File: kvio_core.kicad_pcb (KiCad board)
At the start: 6 copper layers, 98 x 30 mm, 269 parts, among them J1001 12-pin_FFC_(SFV12R), J1301 USB3_B_Micro, J301 Conn_01x06_Male, J401 12-pin_FFC_(SFV12R), J801 12-pin_FFC_(SFV12R), J901 12-pin_FFC_(SFV12R), U1001 IP4254CZ8-4-TTL, U1002 EMI8143, U101 xc7a100t-csg324, U102 ASM330LHH, U1101 AR0135CS, U1201 MT41J128M16JT-125:K, U1301 FT601Q, U1302 EMI8143, U1401 AR0135CS, U201 FAN53541, U202 FAN53541, U203 FAN53541, U204 FAN53541, U301 MX25L6433F, U302 MAX809, U401 EMI8143, U402 IP4254CZ8-4-TTL, U801 IP4254CZ8-4-TTL, U802 EMI8143, U901 IP4254CZ8-4-TTL, U902 EMI8143, Y1301 Crystal_GND24_Small

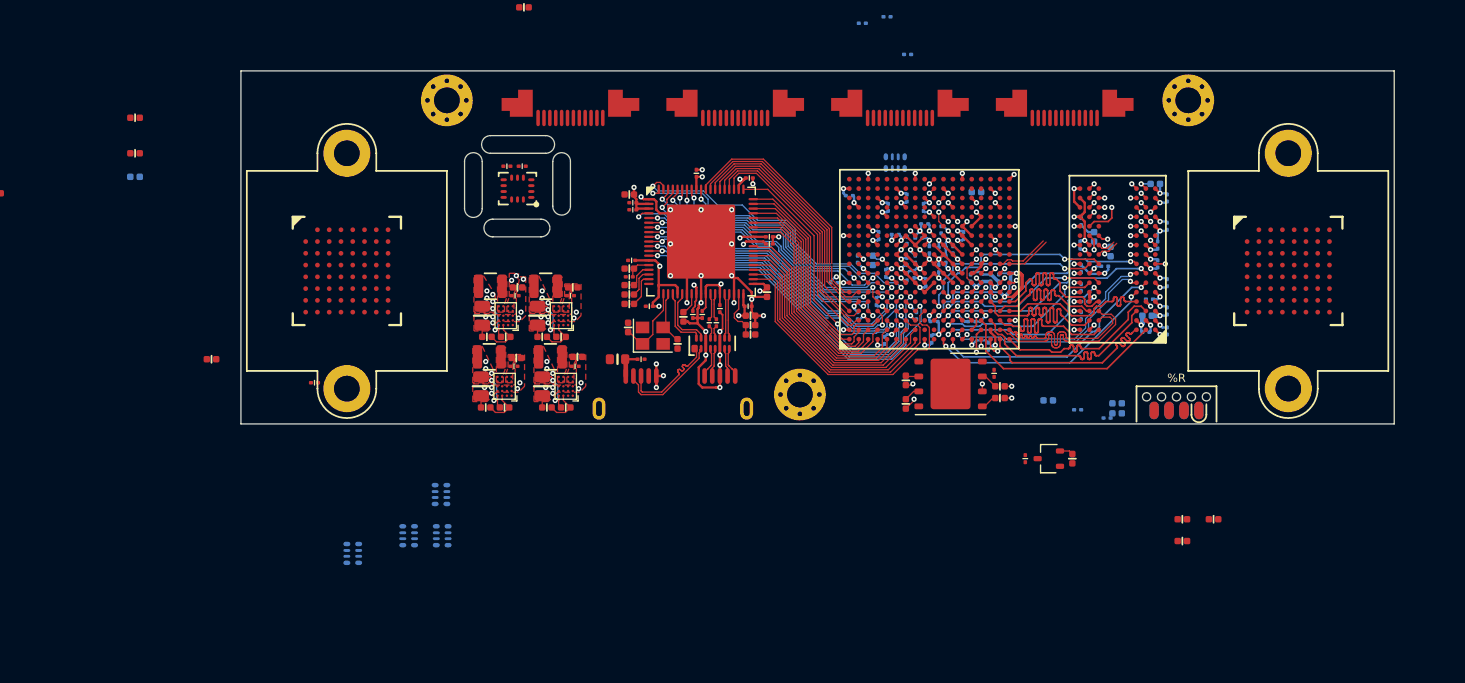
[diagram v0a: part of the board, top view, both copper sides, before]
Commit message: Added IMU + heater, fixed USB3 FIFO lines
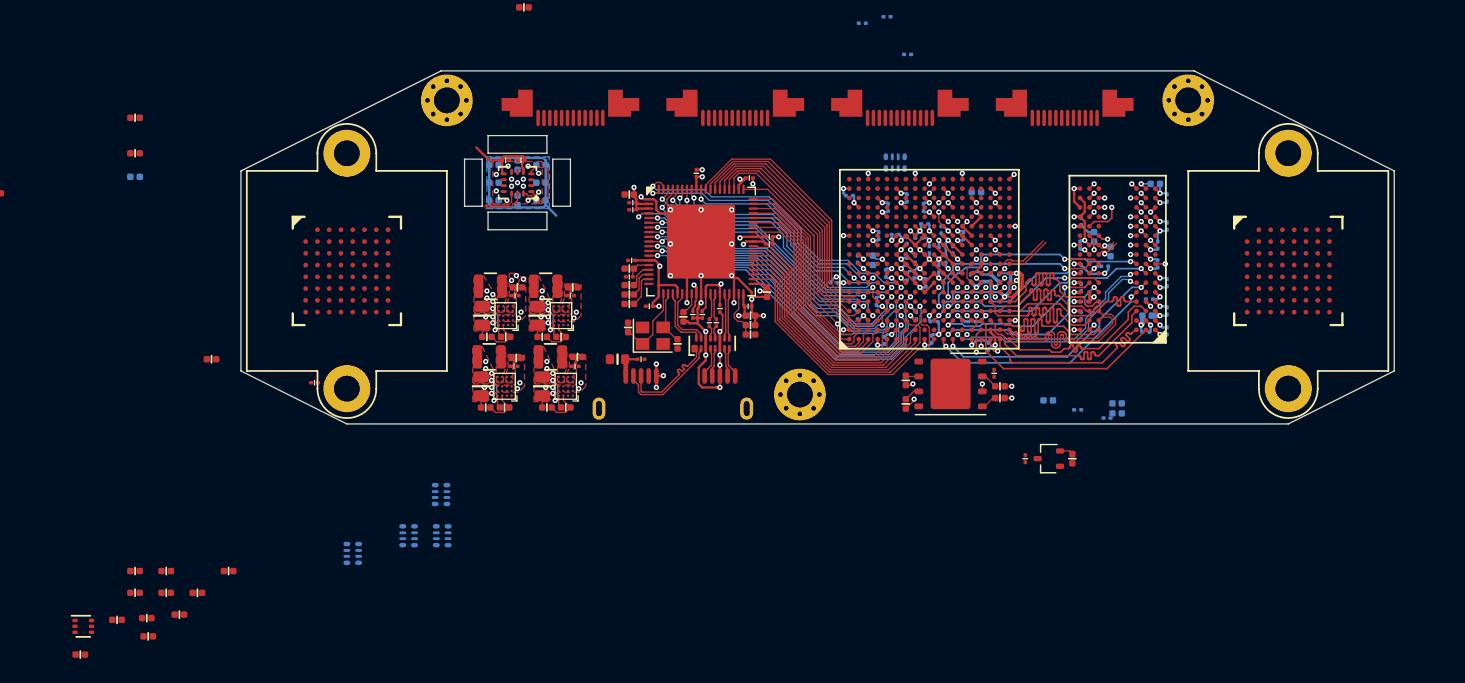
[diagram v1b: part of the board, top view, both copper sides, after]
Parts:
- removed %R: %V, connectors:SOICbiteSmall
- removed C101: 4.7u, passive:C_0402
- removed C102, C103: 0.1u, passive:C_0201
- removed FB101: Ferrite_Bead_Small, passive:R_0402
- removed R101: 4.7k, passive:R_0402
- removed U102: ASM330LHH, lga:LGA-14-2.5x3
- added C1205: 4.7u, passive:C_0402, F.Cu at (139.0, 127.5)
- added C1209: 0.1u, passive:C_0201, F.Cu at (171.8, 92.6)
- added C1222: 0.1u, passive:C_0201, F.Cu at (170.5, 92.6)
- added FB1201: Ferrite_Bead_Small, passive:R_0402, F.Cu at (134.3, 134.6)
- added Q1201: NTZD3155C, sot:SOT-563, F.Cu at (134.6, 132.2)
- added R1206: 100, passive:R_0402, F.Cu at (139.0, 129.3)
- added R1207: 4.7k, passive:R_0402, F.Cu at (137.5, 131.7)
- added R1208: 4.7k, passive:R_0402, F.Cu at (141.7, 127.5)
- added R1209: 180, passive:R_0402, B.Cu at (171.5, 93.0)
- added R1210: 4.7k, passive:R_0402, F.Cu at (141.7, 129.3)
- added R1211: 180, passive:R_0402, B.Cu at (169.5, 94.5)
- added R1212: 180, passive:R_0402, B.Cu at (169.5, 96.0)
- added R1213: 100, passive:R_0402, F.Cu at (140.1, 133.1)
- added R1214: 100, passive:R_0402, F.Cu at (144.3, 129.3)
- added R1215: 100, passive:R_0402, F.Cu at (142.8, 131.2)
- added R1216: 100, passive:R_0402, F.Cu at (146.9, 127.5)
- added R1217: 100, passive:R_0402, F.Cu at (140.0, 131.5)
- added R1218: 180, passive:R_0402, B.Cu at (169.5, 93.0)
- added R1219: 180, passive:R_0402, B.Cu at (173.5, 96.0)
- added R1220: 180, passive:R_0402, B.Cu at (171.5, 96.0)
- added R1221: 180, passive:R_0402, B.Cu at (173.5, 94.5)
- added R1222: 180, passive:R_0402, B.Cu at (173.5, 93.0)
- added U1202: ASM330LHH, lga:LGA-14-2.5x3, F.Cu at (171.5, 94.5)
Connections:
- U101 pad A1: /USB3 Interface/DATA_18 -> /USB3 Interface/DATA_14
- U101 pad A3: /USB3 Interface/DATA_16 -> /USB3 Interface/DATA_17
- U101 pad A4: /USB3 Interface/DATA_15 -> /USB3 Interface/DATA_19
- U101 pad A5: /USB3 Interface/DATA_6 -> /USB3 Interface/DATA_20
- U101 pad A6: /USB3 Interface/DATA_5 -> /USB3 Interface/DATA_22
- U101 pad B1: /USB3 Interface/DATA_17 -> /USB3 Interface/DATA_12
- U101 pad B2: /USB3 Interface/DATA_20 -> /USB3 Interface/DATA_13
- U101 pad B3: /USB3 Interface/DATA_19 -> /USB3 Interface/DATA_16
- U101 pad B4: /USB3 Interface/DATA_14 -> /USB3 Interface/DATA_18
- U101 pad B6: /USB3 Interface/DATA_4 -> /USB3 Interface/DATA_21
- U101 pad B7: /USB3 Interface/DATA_3 -> /USB3 Interface/DATA_23
- U101 pad C1: /USB3 Interface/DATA_31 -> /USB3 Interface/DATA_10
- U101 pad C11: Net-(U101-PadC11) -> /IMU_HEATER
- U101 pad C2: /USB3 Interface/DATA_30 -> /USB3 Interface/DATA_11
- U101 pad C4: /USB3 Interface/DATA_13 -> /USB3 Interface/DATA_28
- U101 pad C5: /USB3 Interface/DATA_2 -> /USB3 Interface/BE_0
- U101 pad C6: /USB3 Interface/DATA_1 -> /USB3 Interface/DATA_29
- U101 pad C7: /USB3 Interface/DATA_8 -> /USB3 Interface/DATA_31
- U101 pad D2: /USB3 Interface/DATA_27 -> /USB3 Interface/DATA_9
- U101 pad D3: /USB3 Interface/DATA_23 -> /USB3 Interface/DATA_15
- U101 pad D4: /USB3 Interface/DATA_22 -> /USB3 Interface/BE_3
- U101 pad D5: /USB3 Interface/DATA_21 -> /USB3 Interface/DATA_26
- U101 pad D7: /USB3 Interface/DATA_12 -> /USB3 Interface/DATA_25
- U101 pad D8: /USB3 Interface/DATA_7 -> /USB3 Interface/DATA_24
- U101 pad E1: /USB3 Interface/BE_3 -> /USB3 Interface/DATA_7
- U101 pad E2: /USB3 Interface/DATA_26 -> /USB3 Interface/DATA_8
- U101 pad E5: /USB3 Interface/DATA_10 -> /USB3 Interface/BE_2
- U101 pad E6: /USB3 Interface/DATA_9 -> /USB3 Interface/BE_1
- U101 pad E7: /USB3 Interface/DATA_11 -> /USB3 Interface/DATA_27
- U101 pad F1: /USB3 Interface/BE_2 -> /USB3 Interface/DATA_6
- U101 pad F3: /USB3 Interface/DATA_25 -> /USB3 Interface/SIWU_N
- U101 pad F4: /USB3 Interface/DATA_24 -> /USB3 Interface/WR_N
- U101 pad F5: /USB3 Interface/DATA_0 -> /USB3 Interface/TXE_N
- U101 pad F6: /USB3 Interface/RXF_N -> /USB3 Interface/DATA_30
- U101 pad G1: /USB3 Interface/BE_1 -> /USB3 Interface/DATA_4
- U101 pad G2: /USB3 Interface/DATA_29 -> /USB3 Interface/DATA_5
- U101 pad G3: /USB3 Interface/WR_N -> /USB3 Interface/DATA_1
- U101 pad G4: /USB3 Interface/SIWU_N -> /USB3 Interface/RXF_N
- U101 pad G6: /USB3 Interface/TXE_N -> /USB3 Interface/RD_N
- U101 pad H1: /USB3 Interface/BE_0 -> /USB3 Interface/DATA_2
- U101 pad H2: /USB3 Interface/DATA_28 -> /USB3 Interface/DATA_3
- U101 pad J4: /USB3 Interface/RD_N -> /USB3 Interface/DATA_0
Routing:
- net /Sensors/IMU_HEATER: track 0.00 -> 19.3 mm
- net /USB3 Interface/DATA_1: track 4.55 -> 23.3 mm, vias 1 -> 0
- net GND: track 145.7 -> 162.0 mm, vias 103 -> 116
- net /USB3 Interface/DATA_3: track 4.87 -> 21.2 mm, vias 1 -> 0
- net /USB3 Interface/DATA_2: track 4.86 -> 20.5 mm, vias 1 -> 0
- net /USB3 Interface/BE_0: track 39.2 -> 24.0 mm, vias 1 -> 2
- net /USB3 Interface/DATA_29: track 37.4 -> 22.4 mm, vias 1 -> 2
- net /USB3 Interface/DATA_5: track 5.51 -> 20.5 mm
- net /USB3 Interface/DATA_0: track 10.6 -> 25.0 mm, vias 1 -> 0
- net /USB3 Interface/DATA_28: track 38.7 -> 24.6 mm, vias 1 -> 2
- net /USB3 Interface/DATA_4: track 6.76 -> 19.8 mm
- net /USB3 Interface/DATA_6: track 6.50 -> 19.1 mm
- net /USB3 Interface/DATA_8: track 9.06 -> 20.6 mm, vias 1 -> 0
- net /USB3 Interface/DATA_7: track 7.45 -> 18.7 mm, vias 1 -> 0
- net /USB3 Interface/BE_1: track 36.9 -> 26.2 mm, vias 1 -> 2
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- added copper zone on B.Cu, net GND
- added copper zone on GND_PWR1, net GND
- added copper zone on GND_PWR3, net GND
- added copper zone on Sig, net GND
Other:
- outline, holes or cut-outs redrawn

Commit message: More layout
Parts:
- added R1105: 1.6k, passive:R_0402, B.Cu at (251.5, 105.7)
- added R1106: 1.6k, passive:R_0402, B.Cu at (254.1, 105.7)
- added R701: 1.6k, passive:R_0402, B.Cu at (151.5, 100.3)
- added R702: 1.6k, passive:R_0402, B.Cu at (151.5, 101.2)
- C1001, C1101, C1102, C1103, C1105, C1106, C1107, C1108, C1109, C1110, C1111, C1112, C1113, C1114, C1115, C1116, C1401, C1402, C1403, C1404, C1405, C1406, C1407, C1408, C1409, C1410, C1411, C1412, C1413, C1414, C1415, C1416, C284, C401, C801, C901, FB1001, FB1101, FB1401, FB401, FB801, FB901, R1001, R1002, R1101, R1102, R1103, R1104, R1402, R801, R802, R901, R902, U1001, U1002, U401, U402, U801, U802, U901, U902: moved to B.Cu
- RN101: moved to F.Cu
- moved C1104 200.7 mm to (251.3, 110.8), turned to 180 degrees
- moved C1107 187.0 mm to (245.2, 118.1), turned to 180 degrees
- moved R1103 186.7 mm to (249.6, 115.0), turned to 180 degrees
- moved FB1101 182.2 mm to (242.6, 118.1), turned to 180 degrees
- moved R1101 181.8 mm to (246.9, 113.2), turned to 180 degrees
- moved R1102 176.9 mm to (244.3, 113.2), turned to 180 degrees
- moved R1104 175.3 mm to (243.1, 107.0), turned to 270 degrees
- moved C1112 168.8 mm to (235.2, 119.8), turned to 180 degrees
- moved C1413 152.4 mm to (260.5, 120.5)
- moved C1414 152.4 mm to (262.8, 120.5)
- moved C1402 152.3 mm to (247.4, 120.4)
- moved C1408 152.3 mm to (250.1, 120.4)
- moved C1401 151.9 mm to (238.5, 120.0)
- moved C1410 150.6 mm to (260.1, 118.7)
- moved C1416 150.6 mm to (257.9, 118.7)
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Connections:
- net Net-(C1001-Pad1) renamed /Camera 4/5V_CAM
- net Net-(C401-Pad1) renamed /Camera 1/5V_CAM
- net Net-(C801-Pad1) renamed /Camera 2/5V_CAM
- net Net-(C901-Pad1) renamed /Camera 3/5V_CAM
- net Net-(J1001-Pad10) renamed /Camera 4/SDA_P
- net Net-(J1001-Pad11) renamed /Camera 4/SCL_P
- net Net-(J1001-Pad2) renamed /Camera 4/D1_P_N
- net Net-(J1001-Pad3) renamed /Camera 4/D1_P_P
- net Net-(J1001-Pad5) renamed /Camera 4/CLK_P_N
- net Net-(J1001-Pad6) renamed /Camera 4/CLK_P_P
- net Net-(J1001-Pad8) renamed /Camera 4/IO1_P
- net Net-(J1001-Pad9) renamed /Camera 4/IO2_P
- net Net-(J401-Pad10) renamed /Camera 1/SDA_P
- net Net-(J401-Pad11) renamed /Camera 1/SCL_P
- net Net-(J401-Pad2) renamed /Camera 1/D1_P_N
- net Net-(J401-Pad3) renamed /Camera 1/D1_P_P
- net Net-(J401-Pad5) renamed /Camera 1/CLK_P_N
- net Net-(J401-Pad6) renamed /Camera 1/CLK_P_P
- net Net-(J401-Pad8) renamed /Camera 1/IO1_P
- net Net-(J401-Pad9) renamed /Camera 1/IO2_P
- net Net-(J801-Pad10) renamed /Camera 2/SDA_P
- net Net-(J801-Pad11) renamed /Camera 2/SCL_P
- net Net-(J801-Pad2) renamed /Camera 2/D1_P_N
- net Net-(J801-Pad3) renamed /Camera 2/D1_P_P
- net Net-(J801-Pad5) renamed /Camera 2/CLK_P_N
- net Net-(J801-Pad6) renamed /Camera 2/CLK_P_P
- net Net-(J801-Pad8) renamed /Camera 2/IO1_P
- net Net-(J801-Pad9) renamed /Camera 2/IO2_P
- net Net-(J901-Pad10) renamed /Camera 3/SDA_P
- net Net-(J901-Pad11) renamed /Camera 3/SCL_P
- net Net-(J901-Pad2) renamed /Camera 3/D1_P_N
- net Net-(J901-Pad3) renamed /Camera 3/D1_P_P
- net Net-(J901-Pad5) renamed /Camera 3/CLK_P_N
- net Net-(J901-Pad6) renamed /Camera 3/CLK_P_P
- net Net-(J901-Pad8) renamed /Camera 3/IO1_P
- net Net-(J901-Pad9) renamed /Camera 3/IO2_P
- net Net-(R1102-Pad1) renamed /sheet5D568411/STANDBY
- net Net-(R1104-Pad1) renamed /sheet5D568411/~OE
- net Net-(R1401-Pad1) renamed /Parallel camera/STANDBY
- net Net-(R1403-Pad1) renamed /Parallel camera/~OE
- RN101 pad 2: /CAM1_CLK_P -> /CAM0_TRIGGER_P
- RN101 pad 3: Net-(RN101-Pad3) -> /CAM1_CLK_P
- RN101 pad 4: Net-(RN101-Pad4) -> /CAM1_TRIGGER_P
- RN101 pad 5: Net-(RN101-Pad5) -> /CAM1_TRIGGER
- RN101 pad 6: Net-(RN101-Pad6) -> /CAM1_CLK
- RN101 pad 7: /CAM1_CLK -> /CAM0_TRIGGER
- RN1101 pad 1: /sheet5D568411/PIXCLK_P -> /CAM1_FLASH
- RN1101 pad 2: Net-(RN1101-Pad2) -> /CAM1_PIXCLK
- RN1101 pad 3: /sheet5D568411/FV_P -> /CAM1_FV
- RN1101 pad 4: /sheet5D568411/LV_P -> /CAM1_LV
- RN1101 pad 5: /CAM1_LV -> /sheet5D568411/LV_P
- RN1101 pad 6: /CAM1_FV -> /sheet5D568411/FV_P
- RN1101 pad 7: Net-(RN1101-Pad7) -> /sheet5D568411/PIXCLK_P
- RN1101 pad 8: /CAM1_PIXCLK -> /sheet5D568411/FLASH_P
- RN1401 pad 1: /Parallel camera/PIXCLK_P -> /CAM0_FLASH
- RN1401 pad 2: Net-(RN1401-Pad2) -> /CAM0_PIXCLK
- RN1401 pad 3: /Parallel camera/FV_P -> /CAM0_FV
- RN1401 pad 4: /Parallel camera/LV_P -> /CAM0_LV
- RN1401 pad 5: /CAM0_LV -> /Parallel camera/LV_P
- RN1401 pad 6: /CAM0_FV -> /Parallel camera/FV_P
- RN1401 pad 7: Net-(RN1401-Pad7) -> /Parallel camera/PIXCLK_P
- RN1401 pad 8: /CAM0_PIXCLK -> /Parallel camera/FLASH_P
- U101 pad B18: /CAM0_TRIGGER -> /CAM0_TRIGGER_P
- U101 pad C16: /CAM1_TRIGGER -> /CAM1_TRIGGER_P
- U101 pad J5: Net-(U101-PadJ5) -> /USB3 Interface/RESET
- U1101 pad E4: /CAM1_FLASH -> /sheet5D568411/FLASH_P
- U1401 pad E4: /CAM0_FLASH -> /Parallel camera/FLASH_P
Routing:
- net +1V8: track 22.0 -> 62.9 mm, vias 16 -> 30
- net /USB3 Interface/RESET: track 2.13 -> 34.8 mm, vias 0 -> 2
- net GND: track 162.0 -> 194.0 mm, vias 116 -> 131
- net VAA: track 0.00 -> 16.4 mm, vias 0 -> 4
- net /sheet5D568411/D0_P: track 0.00 -> 11.4 mm, vias 0 -> 1
- net /Parallel camera/D0_P: track 0.00 -> 11.4 mm, vias 0 -> 1
- net /Parallel camera/LV_P: track 0.00 -> 10.9 mm, vias 0 -> 1
- net /sheet5D568411/LV_P: track 0.00 -> 10.9 mm, vias 0 -> 1
- net /sheet5D568411/D4_P: track 0.00 -> 10.8 mm, vias 0 -> 1
- net /Parallel camera/D4_P: track 0.00 -> 10.8 mm, vias 0 -> 1
- net /sheet5D568411/D8_P: track 0.00 -> 10.7 mm, vias 0 -> 1
- net /Parallel camera/D8_P: track 0.00 -> 10.7 mm, vias 0 -> 1
- net /sheet5D568411/FV_P: track 0.00 -> 10.4 mm, vias 0 -> 1
- net /Parallel camera/FV_P: track 0.00 -> 10.4 mm, vias 0 -> 1
- net /sheet5D568411/D1_P: track 0.00 -> 10.1 mm, vias 0 -> 1
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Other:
- outline, holes or cut-outs redrawn
- board text added: "K"
- board text added: "Vision"
- board text added: "Visual Inertial Accelerator Rev. A"

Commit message: More work
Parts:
- removed C1304: 0.1u, passive:C_0201
- added U303: SOICbite_JTAG, connectors:SOICbiteSmall, F.Cu at (217.3, 114.6)
- J301: footprint Connector_PinSocket_1.27mm:PinSocket_2x03_P1.27mm_Vertical_SMD -> Connector_PinSocket_1.27mm:PinSocket_2x03_P1.27mm_Vertical
- moved R317 83.4 mm to (200.5, 117.0)
- moved R318 83.4 mm to (201.5, 117.0)
- moved R319 83.4 mm to (202.5, 117.0)
- moved R320 83.4 mm to (203.5, 117.0)
- moved J301 82.9 mm to (202.5, 113.3), turned to 270 degrees
- moved Q1201 7.23 mm to (178.6, 106.3)
- moved R1206 7.23 mm to (178.6, 103.9)
- moved R1207 7.23 mm to (178.6, 104.8)
- moved R1208 7.23 mm to (178.6, 107.8)
- moved R304 3.21 mm to (207.3, 95.1), turned to 270 degrees
- moved C243 1.00 mm to (201.2, 99.0)
- moved C1209 0.71 mm to (172.3, 93.6)
- moved C1222 0.71 mm to (171.0, 93.6)
- moved R1209 0.71 mm to (172.0, 94.0)
- moved R1211 0.71 mm to (170.0, 95.5)
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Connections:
- R1303 pad 1: +3V3 -> GND
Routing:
- net /Config/CFG_D1: track 1.21 -> 16.4 mm
- net /Config/CFG_CLK: track 0.64 -> 15.3 mm, vias 1 -> 2
- net /Config/CFG_D0: track 1.17 -> 15.0 mm
- net GND: track 194.0 -> 206.3 mm, vias 131 -> 133
- net /Config/CFG_CS: track 1.37 -> 13.1 mm
- net /Config/CFG_D3: track 1.17 -> 11.1 mm
- net /Config/CFG_D2: track 1.66 -> 11.5 mm
- net +1V8: track 62.9 -> 58.4 mm
- net /Sensors/IMU_INT_P: track 5.80 -> 3.53 mm
- net /USB3 Interface/DATA_0: track 25.0 -> 26.1 mm
- net /USB3 Interface/DATA_1: track 23.3 -> 24.3 mm
- net /USB3 Interface/DATA_2: track 20.5 -> 21.4 mm
- net /USB3 Interface/DATA_3: track 21.2 -> 22.0 mm
- net /USB3 Interface/RESET: track 34.8 -> 35.5 mm
- net /USB3 Interface/DATA_4: track 19.8 -> 20.6 mm
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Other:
- outline, holes or cut-outs redrawn

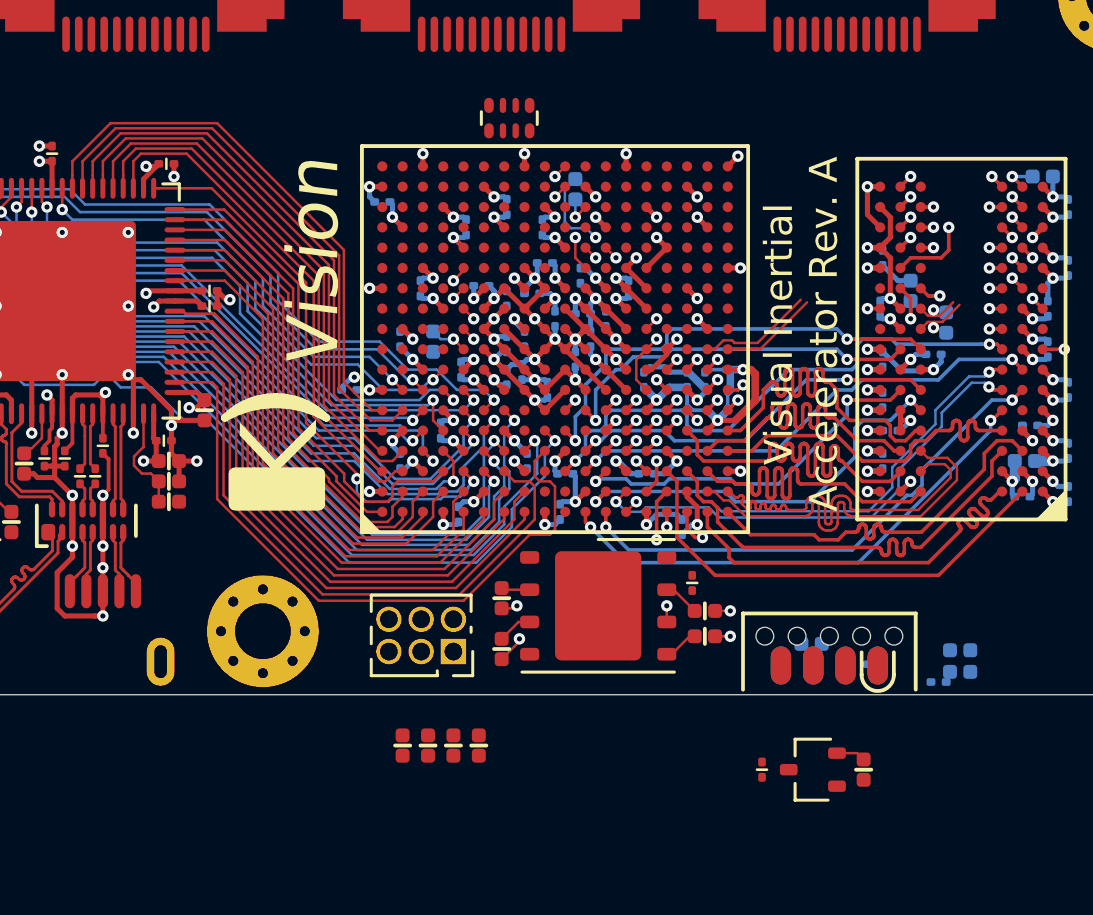
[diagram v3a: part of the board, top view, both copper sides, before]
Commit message: Added signal for global clock
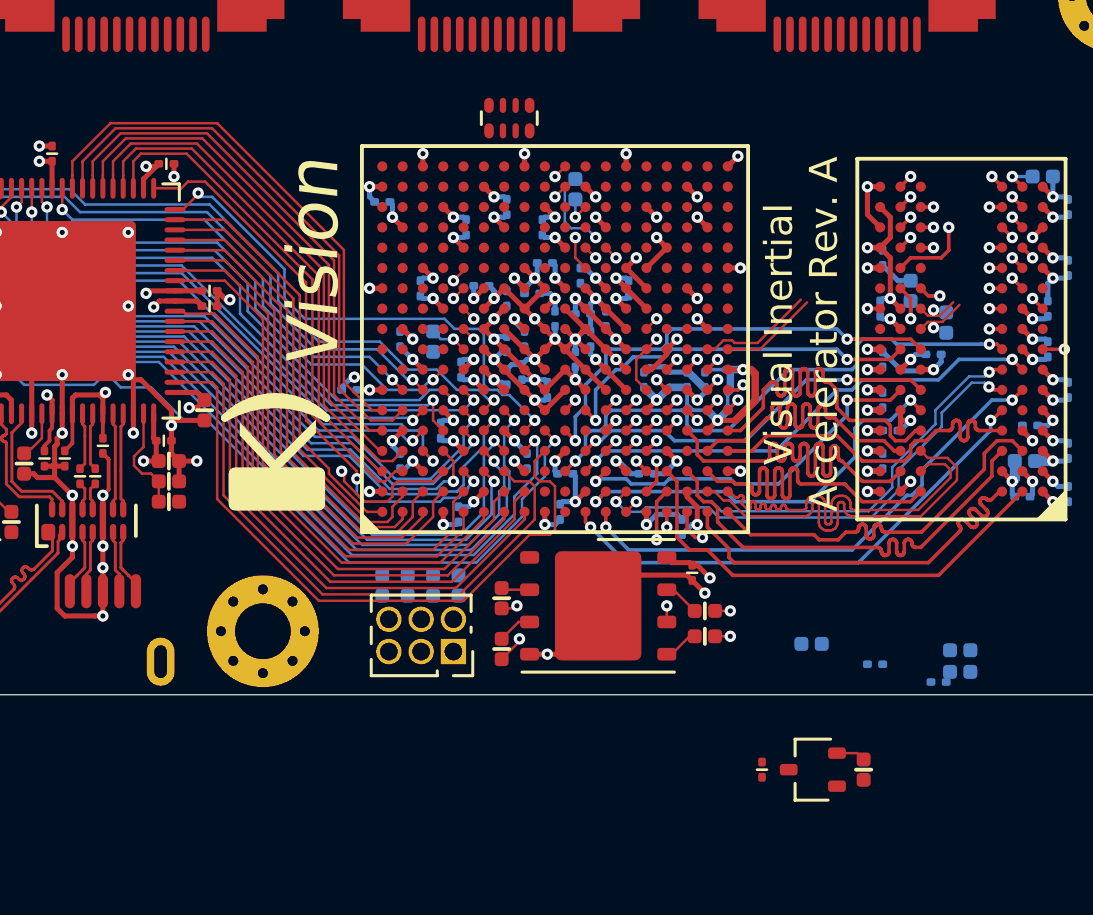
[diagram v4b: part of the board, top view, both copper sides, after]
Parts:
- removed U303: SOICbite_JTAG, connectors:SOICbiteSmall
- R317, R318, R319, R320: moved to B.Cu
- moved R317 6.35 mm to (199.7, 110.7), turned to 270 degrees
- moved R318 6.35 mm to (200.7, 110.7), turned to 270 degrees
- moved R319 6.35 mm to (201.7, 110.7), turned to 270 degrees
- moved R320 6.35 mm to (202.7, 110.7), turned to 270 degrees
- moved C301 0.40 mm to (211.9, 110.2)
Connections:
- U101 pad D3: /USB3 Interface/DATA_15 -> /USB3 Interface/GLCLK_100MHZ
- U101 pad H5: Net-(U101-PadH5) -> /USB3 Interface/DATA_15
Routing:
- net GND: track 206.3 -> 215.8 mm, vias 133 -> 135
- net /USB3 Interface/GLCLK_100MHZ: track 0.00 -> 5.40 mm, vias 0 -> 1
- net +3V3: track 38.5 -> 40.5 mm, vias 26 -> 27
- net /USB3 Interface/DATA_15: track 19.6 -> 20.6 mm, vias 0 -> 2
